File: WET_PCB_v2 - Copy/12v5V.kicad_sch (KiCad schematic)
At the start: 3 parts, among them U6 L7805

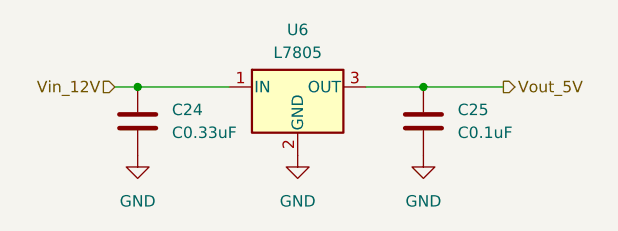
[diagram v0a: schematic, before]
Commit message: microcontroller to chip traces done
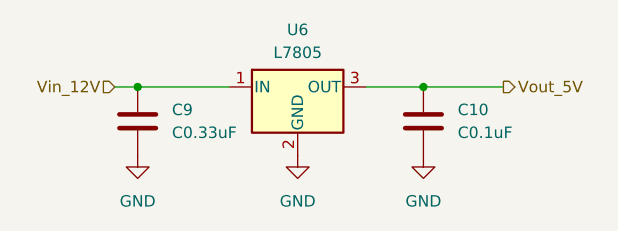
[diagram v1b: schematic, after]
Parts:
- renumbered C25 to C10, C24 to C9
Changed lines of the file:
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@@
 		(dnp no)
 		(fields_autoplaced yes)
-		(property "Reference" "#PWR057"
+		(property "Reference" "#PWR061"
 			(at 62.23 39.37 0)
 			(hide yes)
@@
 			(project "WET_PCB_v2"
 				(path "/13451c35-1666-47d9-9525-8d8125ba1cf3/7293ed87-9a5c-4e01-a7da-6a6e465a8771"
-					(reference "#PWR057")
+					(reference "#PWR061")
 					(unit 1)
 				)
@@
 		(dnp no)
 		(fields_autoplaced yes)
-		(property "Reference" "#PWR058"
+		(property "Reference" "#PWR063"
 			(at 76.2 39.37 0)
 			(hide yes)
@@
 			(project "WET_PCB_v2"
 				(path "/13451c35-1666-47d9-9525-8d8125ba1cf3/7293ed87-9a5c-4e01-a7da-6a6e465a8771"
-					(reference "#PWR058")
+					(reference "#PWR063")
 					(unit 1)
 				)
@@
 		(dnp no)
 		(fields_autoplaced yes)
-		(property "Reference" "C24"
+		(property "Reference" "C9"
 			(at 48.26 27.9399 0)
 			(show_name no)
@@
 			(project "WET_PCB_v2"
 				(path "/13451c35-1666-47d9-9525-8d8125ba1cf3/7293ed87-9a5c-4e01-a7da-6a6e465a8771"
-					(reference "C24")
+					(reference "C9")
 					(unit 1)
 				)
@@
 		(dnp no)
 		(fields_autoplaced yes)
-		(property "Reference" "C25"
+		(property "Reference" "C10"
 			(at 80.01 27.9399 0)
 			(show_name no)
@@
 			(project "WET_PCB_v2"
 				(path "/13451c35-1666-47d9-9525-8d8125ba1cf3/7293ed87-9a5c-4e01-a7da-6a6e465a8771"
-					(reference "C25")
+					(reference "C10")
 					(unit 1)
 				)
@@
 		(dnp no)
 		(fields_autoplaced yes)
-		(property "Reference" "#PWR056"
+		(property "Reference" "#PWR062"
 			(at 44.45 39.37 0)
 			(hide yes)
@@
 			(project "WET_PCB_v2"
 				(path "/13451c35-1666-47d9-9525-8d8125ba1cf3/7293ed87-9a5c-4e01-a7da-6a6e465a8771"
-					(reference "#PWR056")
-					(unit 1)
-				)
+					(reference "#PWR062")
+					(unit 1)
+				)
